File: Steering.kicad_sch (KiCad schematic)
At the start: 1 part, among them J5(SteeringWheel) 776280-1 (Blue one)

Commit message: Digital IO, Relay, and Switchbox changes
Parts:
- added R1, R10, R11, R12, R13, R14, R2, R5, R6, R7, R8, R9: 10K, symbol Device:R_US
- added U1, U2, U5, U6, U7, U8: VOM618A-3T, VOM618A-3T:SOIC254P695X242-4N, symbol VOM618A-3T:VOM618A-3T
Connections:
- net at J5(SteeringWheel).2: now also R2.1
- net at J5(SteeringWheel).3: now also R5.1
- net at J5(SteeringWheel).4: now also R7.1
- net at J5(SteeringWheel).5: now also R9.1
- net at J5(SteeringWheel).6: now also R11.1
- net +3.3 renamed +12V
- net GasPedal: no longer names the net of J5(SteeringWheel).8
- new net: R5.2, U2.1
- new net: R7.2, U5.1
- new net: R9.2, U6.1
- new net: R13.2, U8.1
- new net: R2.2, U1.1
- new net: R11.2, U7.1
- new net +3.3V: R1.2, R10.2, R12.2, R14.2, R6.2, R8.2
- new net Brake: R14.1, U8.4
- new net Dio0: R1.1, U1.4
- new net Dio1: R6.1, U2.4
- new net Dio2: R8.1, U5.4
- new net Dio3: R10.1, U6.4
- new net Dio4: R12.1, U7.4
- new net GND: U1.3, U2.3, U5.3, U6.3, U7.3, U8.3
- new net GNDp: U1.2, U2.2, U5.2, U6.2, U7.2, U8.2
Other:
- moved on the sheet: J5(SteeringWheel)

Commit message: Fixed ERC errors and warnings
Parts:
- added J14: 2-1445057-2, 2-1445057-2:TE_2-1445057-2, symbol 2-1445057-2:2-1445057-2
- renumbered J5(SteeringWheel) to J5(SteeringWheel)1
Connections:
- net +12V: now also J14.1
- net at R13.1: now also J14.2
- no-connect marks 0 -> 2

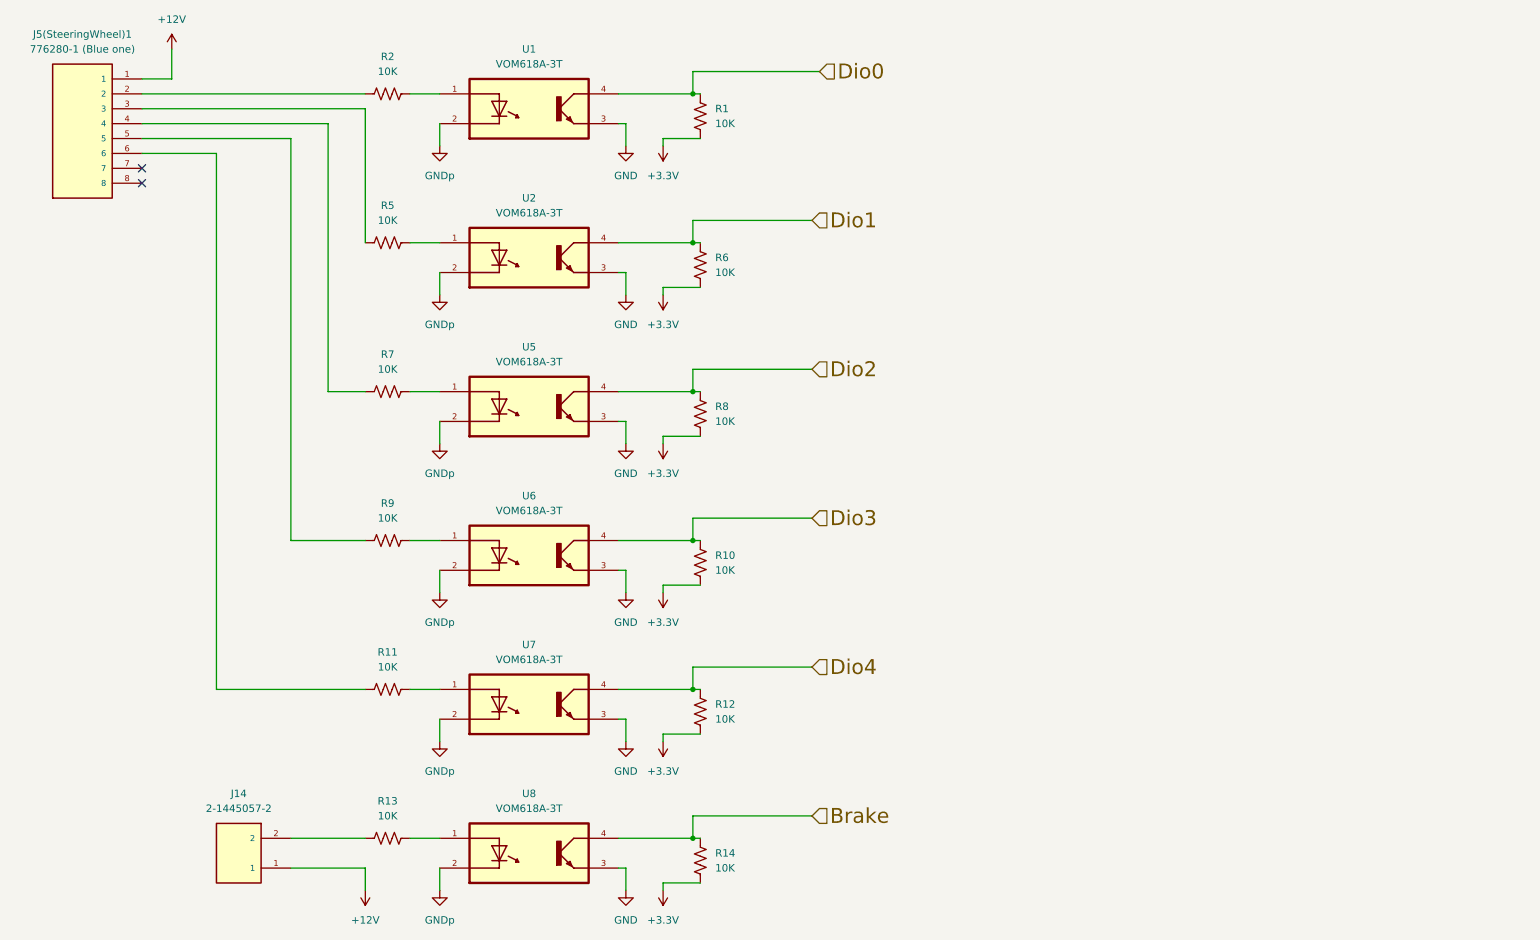
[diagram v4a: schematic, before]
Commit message: Moved everything to 23-POS AmpSeal
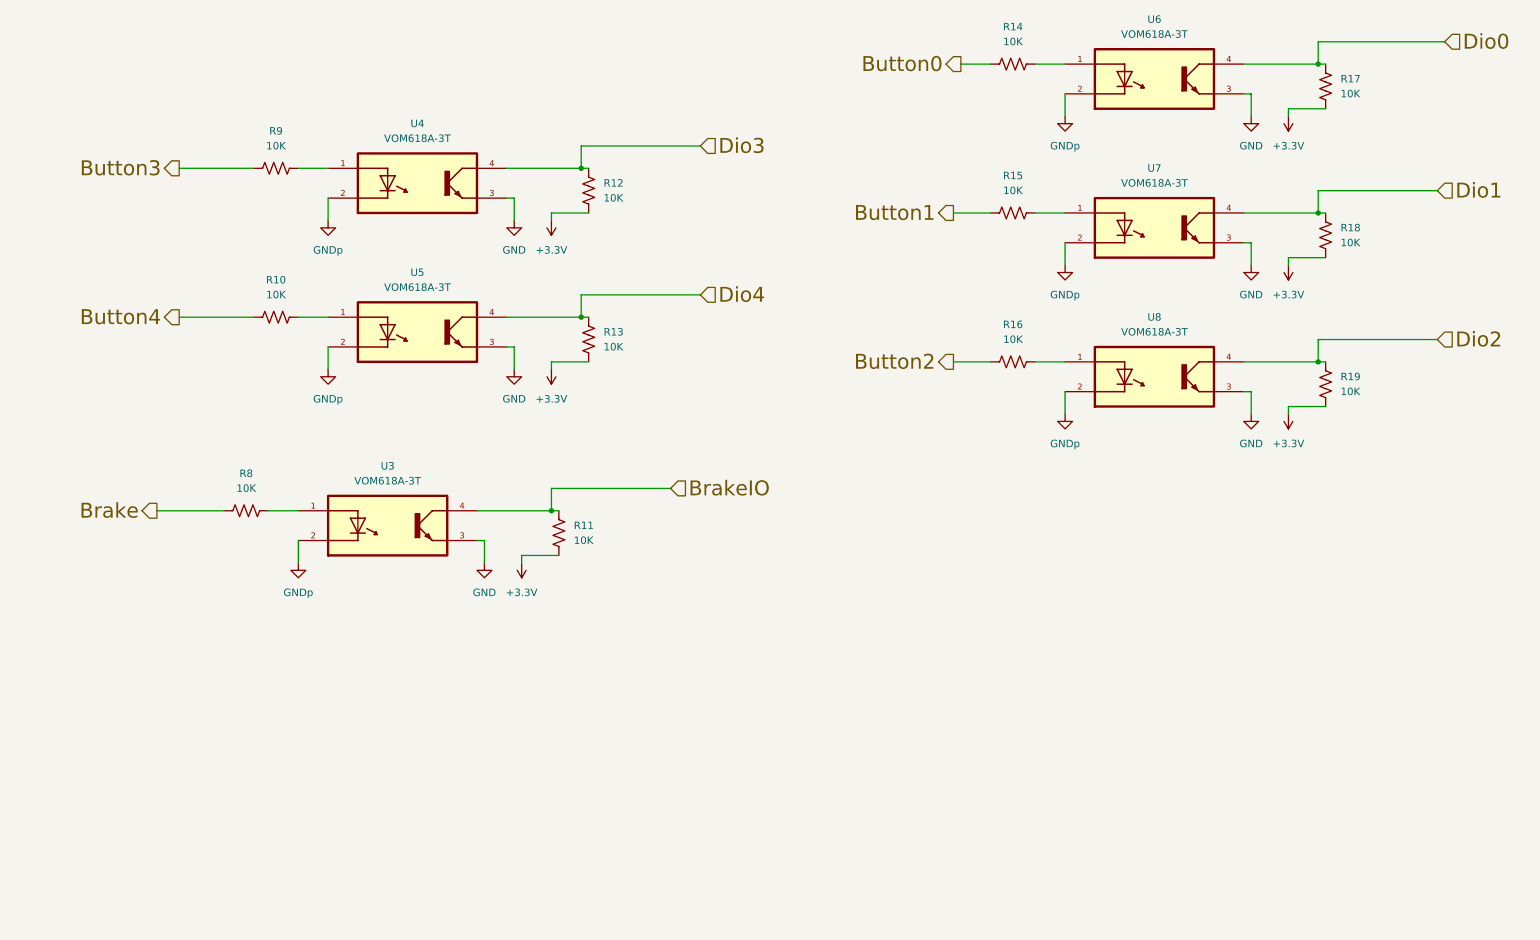
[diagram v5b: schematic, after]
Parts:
- removed J14: 2-1445057-2, 2-1445057-2:TE_2-1445057-2, symbol 2-1445057-2:2-1445057-2
- removed J5(SteeringWheel)1: 776280-1 (Blue one), 776280-1:TE_776280-1, symbol 776280-1:776280-1
- renumbered R11 to R10, R14 to R11, R10 to R12, R12 to R13, R2 to R14, R5 to R15, R7 to R16, R1 to R17, R6 to R18, R8 to R19, R13 to R8, U8 to U3, U6 to U4, U7 to U5, U1 to U6, U2 to U7, U5 to U8
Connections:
- net Brake: now also R8.1; no longer R11.1, U3.4
- net Button1: now reaches R15.1
- net Button3: now reaches R9.1
- net Button0: now reaches R14.1
- net Button2: now reaches R16.1
- net Button4: now reaches R10.1
- new net BrakeIO: R11.1, U3.4
- no-connect marks 2 -> 0
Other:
- moved on the sheet: R10, R11, R12, R13, R14, R15, R16, R17, R18, R19, R8, R9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

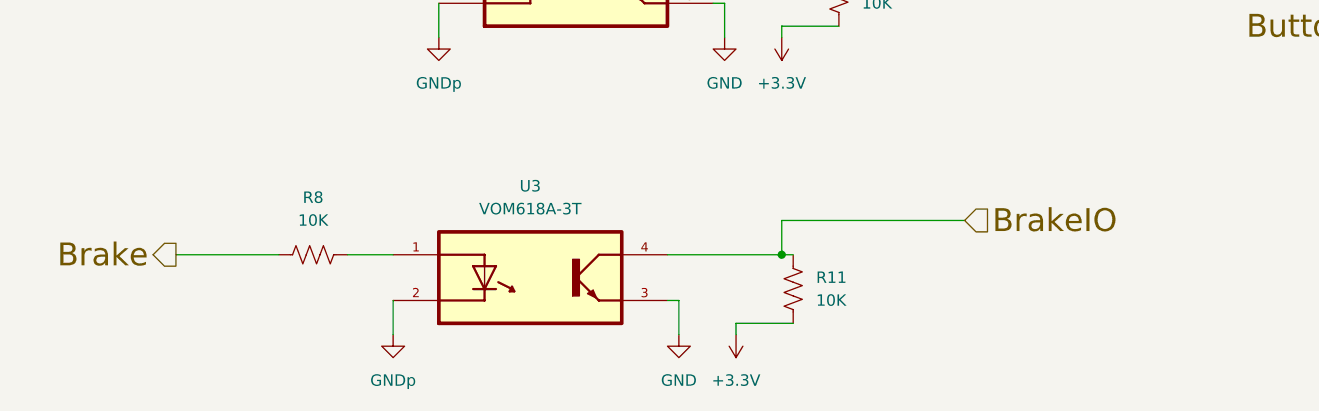
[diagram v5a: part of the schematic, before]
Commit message: Final Pinout for connectors
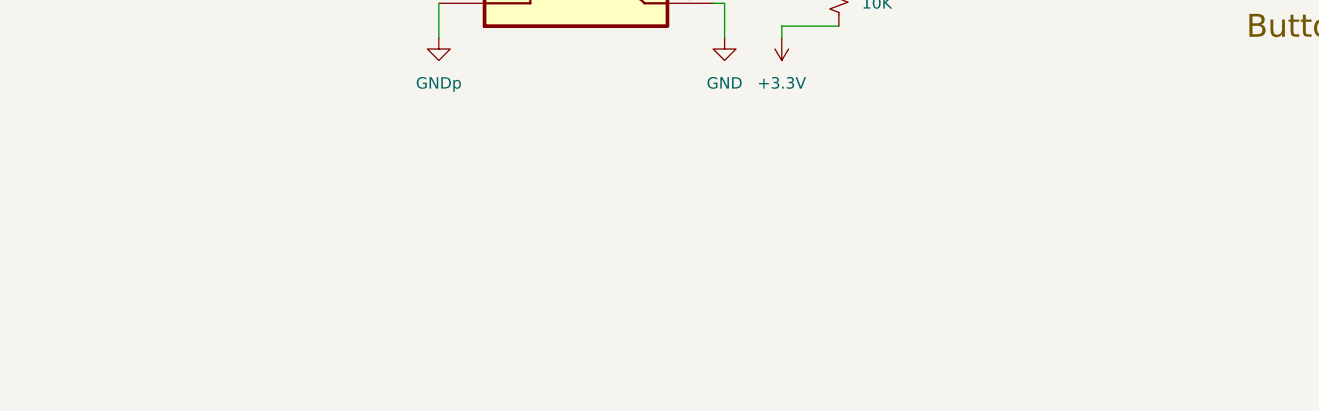
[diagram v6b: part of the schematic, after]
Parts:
- removed R11, R8: 10K, symbol Device:R_US
- removed U3: VOM618A-3T, VOM618A-3T:SOIC254P695X242-4N, symbol VOM618A-3T:VOM618A-3T

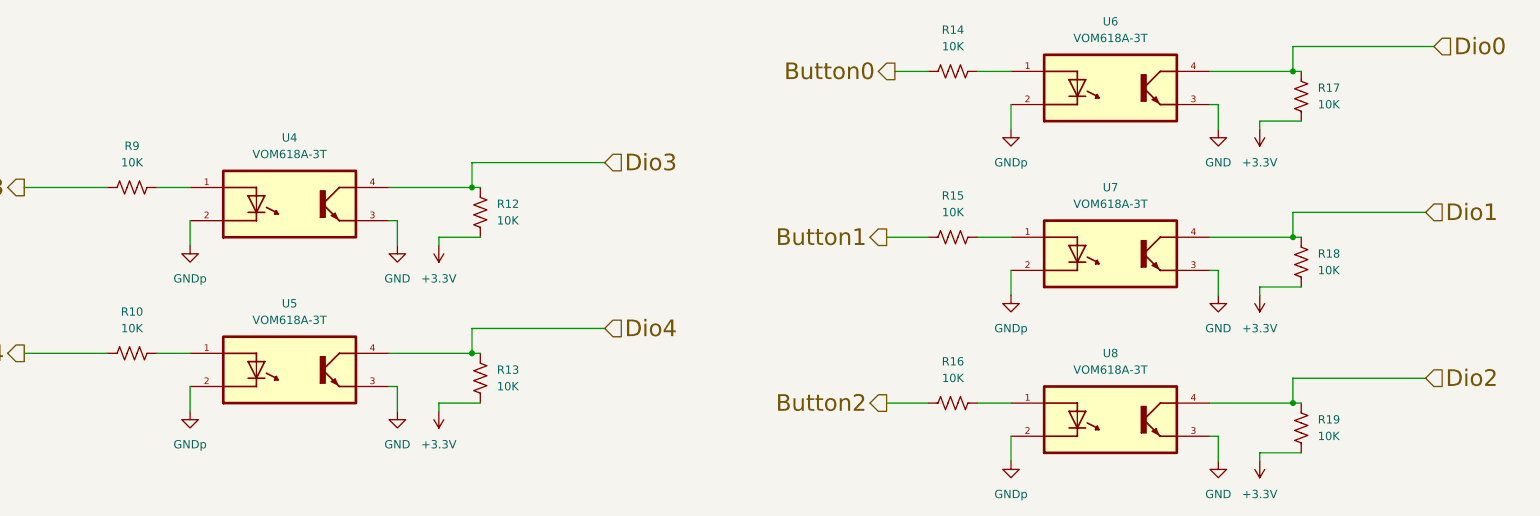
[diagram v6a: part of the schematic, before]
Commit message: made connector match drawing
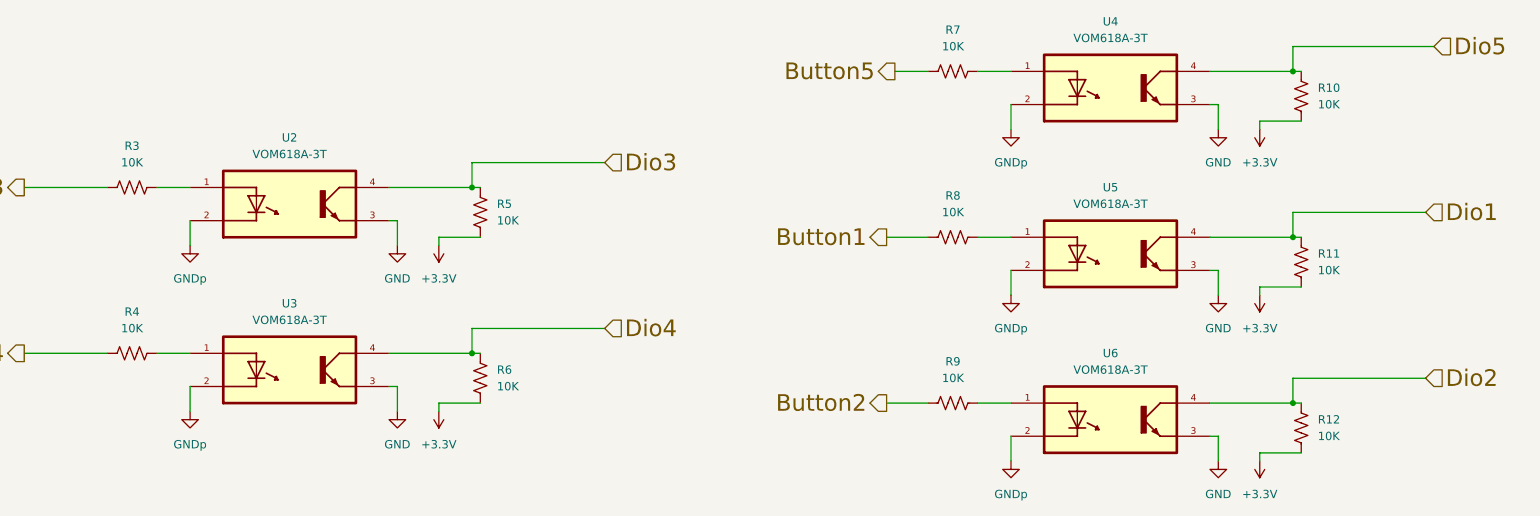
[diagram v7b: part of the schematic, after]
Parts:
- renumbered R17 to R10, R18 to R11, R19 to R12, R9 to R3, R10 to R4, R12 to R5, R13 to R6, R14 to R7, R15 to R8, R16 to R9, U4 to U2, U5 to U3, U6 to U4, U7 to U5, U8 to U6
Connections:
- net Button0 renamed Button5
- net Dio0 renamed Dio5

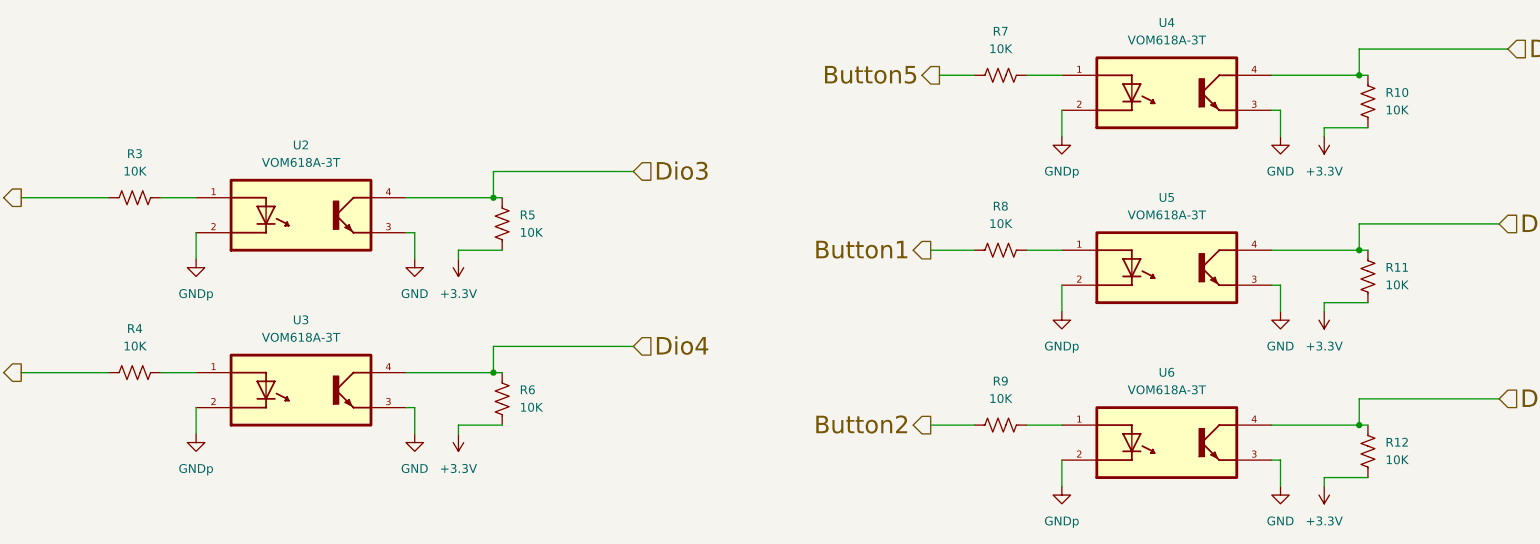
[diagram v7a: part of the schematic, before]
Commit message: placed most components
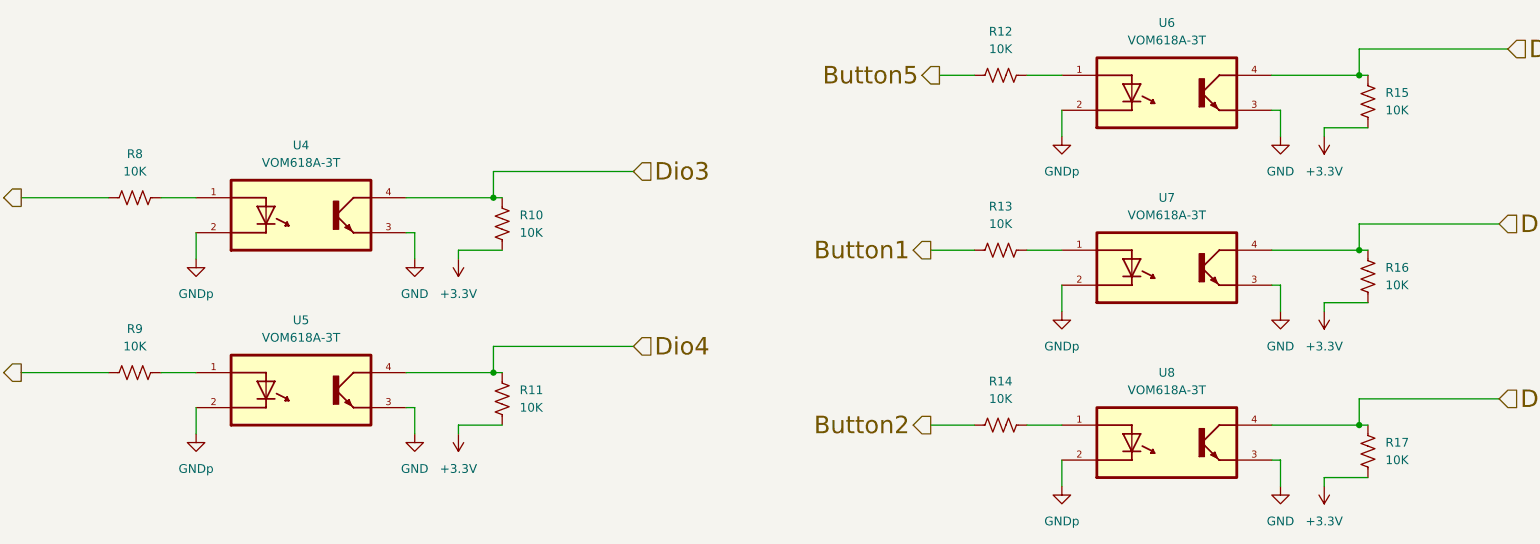
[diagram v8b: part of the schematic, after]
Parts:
- R10: renamed from R5; footprint (none) -> Resistor_SMD:R_0805_2012Metric
- R11: renamed from R6; footprint (none) -> Resistor_SMD:R_0805_2012Metric
- R12: renamed from R7; footprint (none) -> Resistor_SMD:R_0805_2012Metric
- R13: renamed from R8; footprint (none) -> Resistor_SMD:R_0805_2012Metric
- R14: renamed from R9; footprint (none) -> Resistor_SMD:R_0805_2012Metric
- R15: renamed from R10; footprint (none) -> Resistor_SMD:R_0805_2012Metric
- R16: renamed from R11; footprint (none) -> Resistor_SMD:R_0805_2012Metric
- R17: renamed from R12; footprint (none) -> Resistor_SMD:R_0805_2012Metric
- R8: renamed from R3; footprint (none) -> Resistor_SMD:R_0805_2012Metric
- R9: renamed from R4; footprint (none) -> Resistor_SMD:R_0805_2012Metric
- renumbered U2 to U4, U3 to U5, U4 to U6, U5 to U7, U6 to U8
